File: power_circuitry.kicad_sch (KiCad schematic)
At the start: 29 parts, among them U3 MCP6007, U4 MCP6007, U5 MCP6007

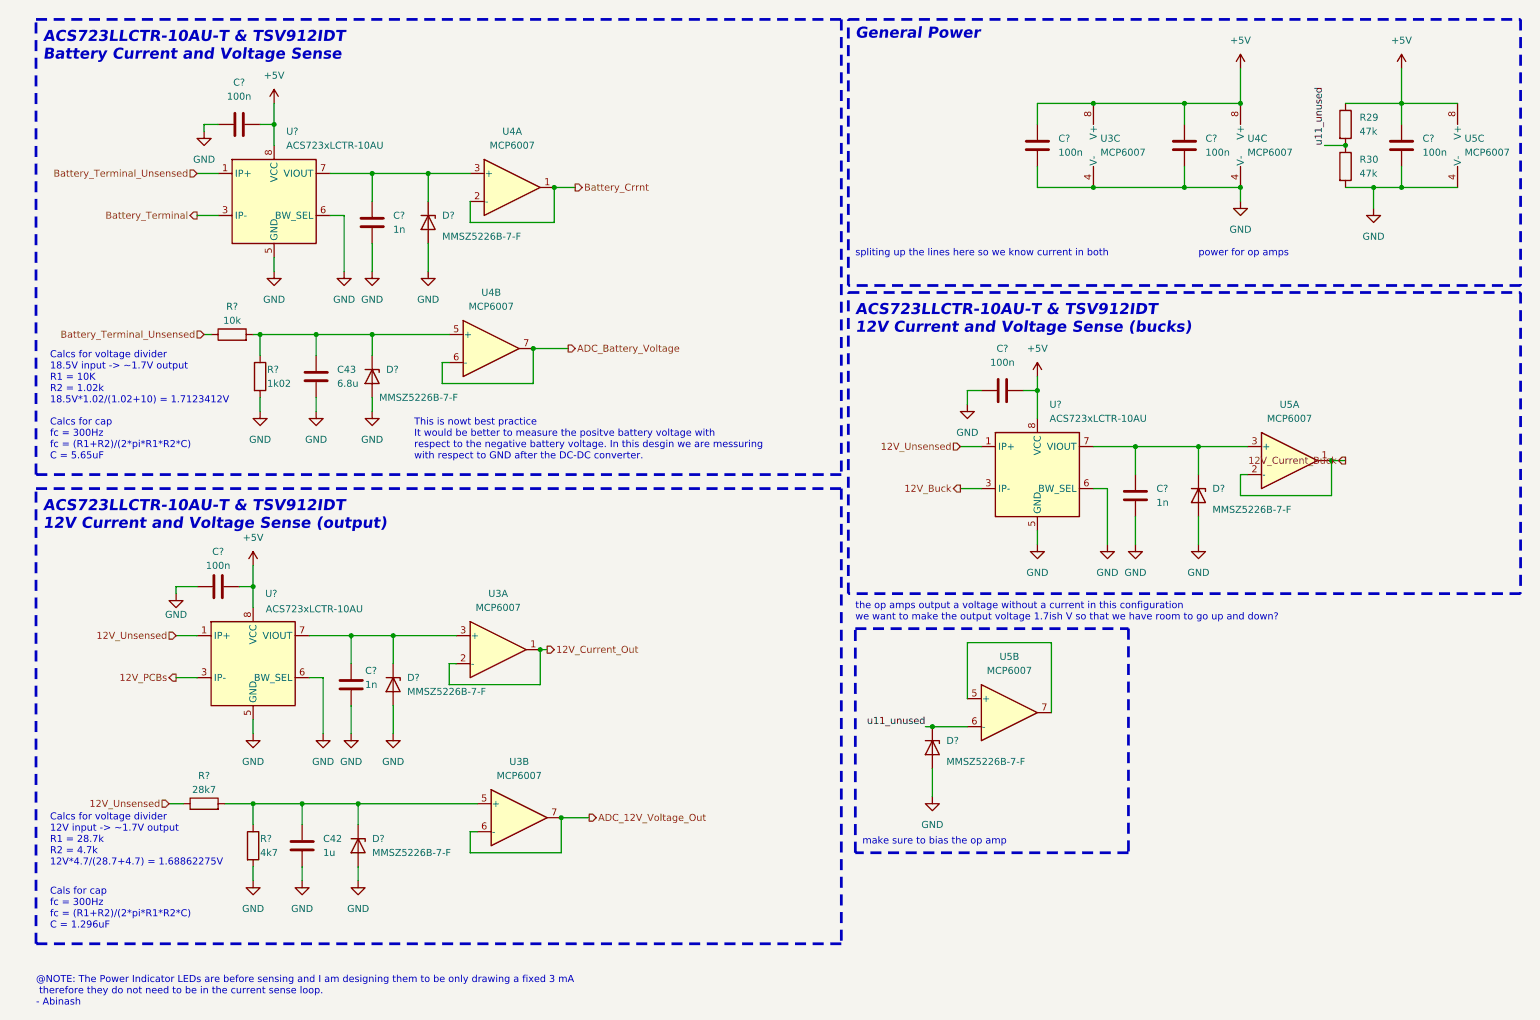
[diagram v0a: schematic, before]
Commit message: buck converter updates
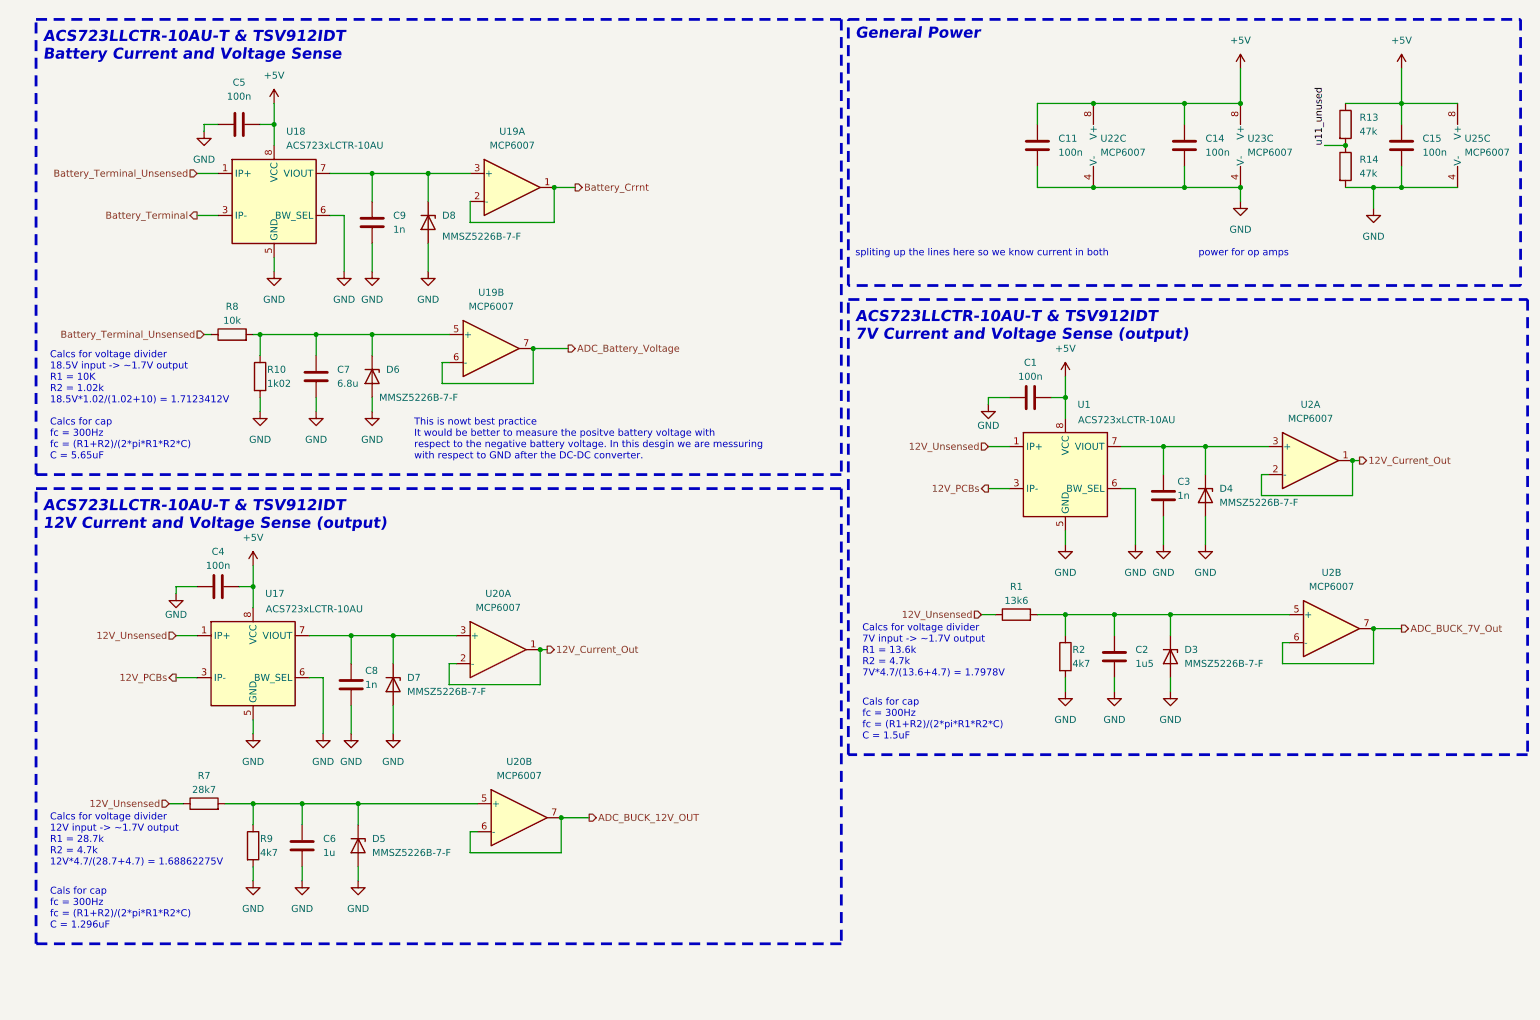
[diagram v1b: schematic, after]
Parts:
- removed C?: 1n, Capacitor_SMD:C_0402_1005Metric, symbol Device:C
- removed C?: 100n, Capacitor_SMD:C_0603_1608Metric, symbol Device:C
- removed D? (x2): MMSZ5226B-7-F, Diode_SMD:D_SOD-123, symbol Device:D_Zener
- removed unit 1 of U5
- removed unit 2 of U5
- removed U?: ACS723xLCTR-10AU, Package_SO:SOIC-8_3.9x4.9mm_P1.27mm, symbol Sensor_Current:ACS723xLCTR-10AU
- added C1: 100n, Capacitor_SMD:C_0603_1608Metric, symbol Device:C
- added C2: 1u5, Capacitor_SMD:C_0603_1608Metric, symbol Device:C
- added C3: 1n, Capacitor_SMD:C_0402_1005Metric, symbol Device:C
- added D3, D4: MMSZ5226B-7-F, Diode_SMD:D_SOD-123, symbol Device:D_Zener
- added R1: 13k6, Resistor_SMD:R_0603_1608Metric, symbol Device:R
- added R2: 4k7, Resistor_SMD:R_0603_1608Metric, symbol Device:R
- added U1: ACS723xLCTR-10AU, Package_SO:SOIC-8_3.9x4.9mm_P1.27mm, symbol Sensor_Current:ACS723xLCTR-10AU
- added U2: MCP6007, Package_SO:SOIC-8_3.9x4.9mm_P1.27mm, symbol ecocad_lib_symbols:MCP6007
- C5: renamed from C?; footprint Capacitor_SMD:C_0402_1005Metric -> Capacitor_SMD:C_0603_1608Metric
- U22: renamed from U3; footprint BP_FTP:SO8_STM -> Package_SO:SOIC-8_3.9x4.9mm_P1.27mm
- U23: renamed from U4; footprint BP_FTP:SO8_STM -> Package_SO:SOIC-8_3.9x4.9mm_P1.27mm
- U25: renamed from U5; footprint BP_FTP:SO8_STM -> Package_SO:SOIC-8_3.9x4.9mm_P1.27mm
- gave numbers to parts that had none: 16
- renumbered C42 to C6, C43 to C7, R29 to R13, R30 to R14, U4 to U19, U3 to U20
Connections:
- net +5V: now also C1.1, U1.8 (VCC)
- net 12V_Current_Out: now also U2.1, U2.2 (-)
- net 12V_PCBs: now also U1.3 (IP-), U1.4 (IP-)
- net 12V_Unsensed: now also R1.1, U1.1 (IP+), U1.2 (IP+)
- net GND: now also C1.2, C2.2, C3.2, D3.2 (A), D4.2 (A), R2.2, U1.5 (GND), U1.6 (BW_SEL)
- net ADC_12V_Voltage_Out renamed ADC_BUCK_12V_OUT
- new net: C3.1, D4.1 (K), U1.7 (VIOUT), U2.3 (+)
- new net: C2.1, D3.1 (K), R1.2, R2.1, U2.5 (+)
- new net ADC_BUCK_7V_Out: U2.6 (-), U2.7
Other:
- note added: "ACS723LLCTR-10AU-T & TSV912IDT 7V Current and Voltage Sense (output)"
- note added: "Calcs for voltage divider 7V input -> ~1.7V output R1 = 13.6k R2 = 4.7k 7V*4.7/(13.6+4.7) = 1.7978V"
- note added: "Cals for cap fc = 300Hz fc = (R1+R2)/(2*pi*R1*R2*C) C = 1.5uF"
- note removed: "@NOTE: The Power Indicator LEDs are before sensing and I am designing them to be only drawing a fixed 3 mA therefore they do not need to be in the current sense loop. - Abinash"
- note removed: "ACS723LLCTR-10AU-T & TSV912IDT 12V Current and Voltage Sense (bucks)"
- note removed: "make sure to bias the op amp"
- note removed: "the op amps output a voltage without a current in this configuration we want to make the output voltage 1.7ish V so that we have room to go up and down?"

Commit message: MCU and Schematic Hierarchy updates
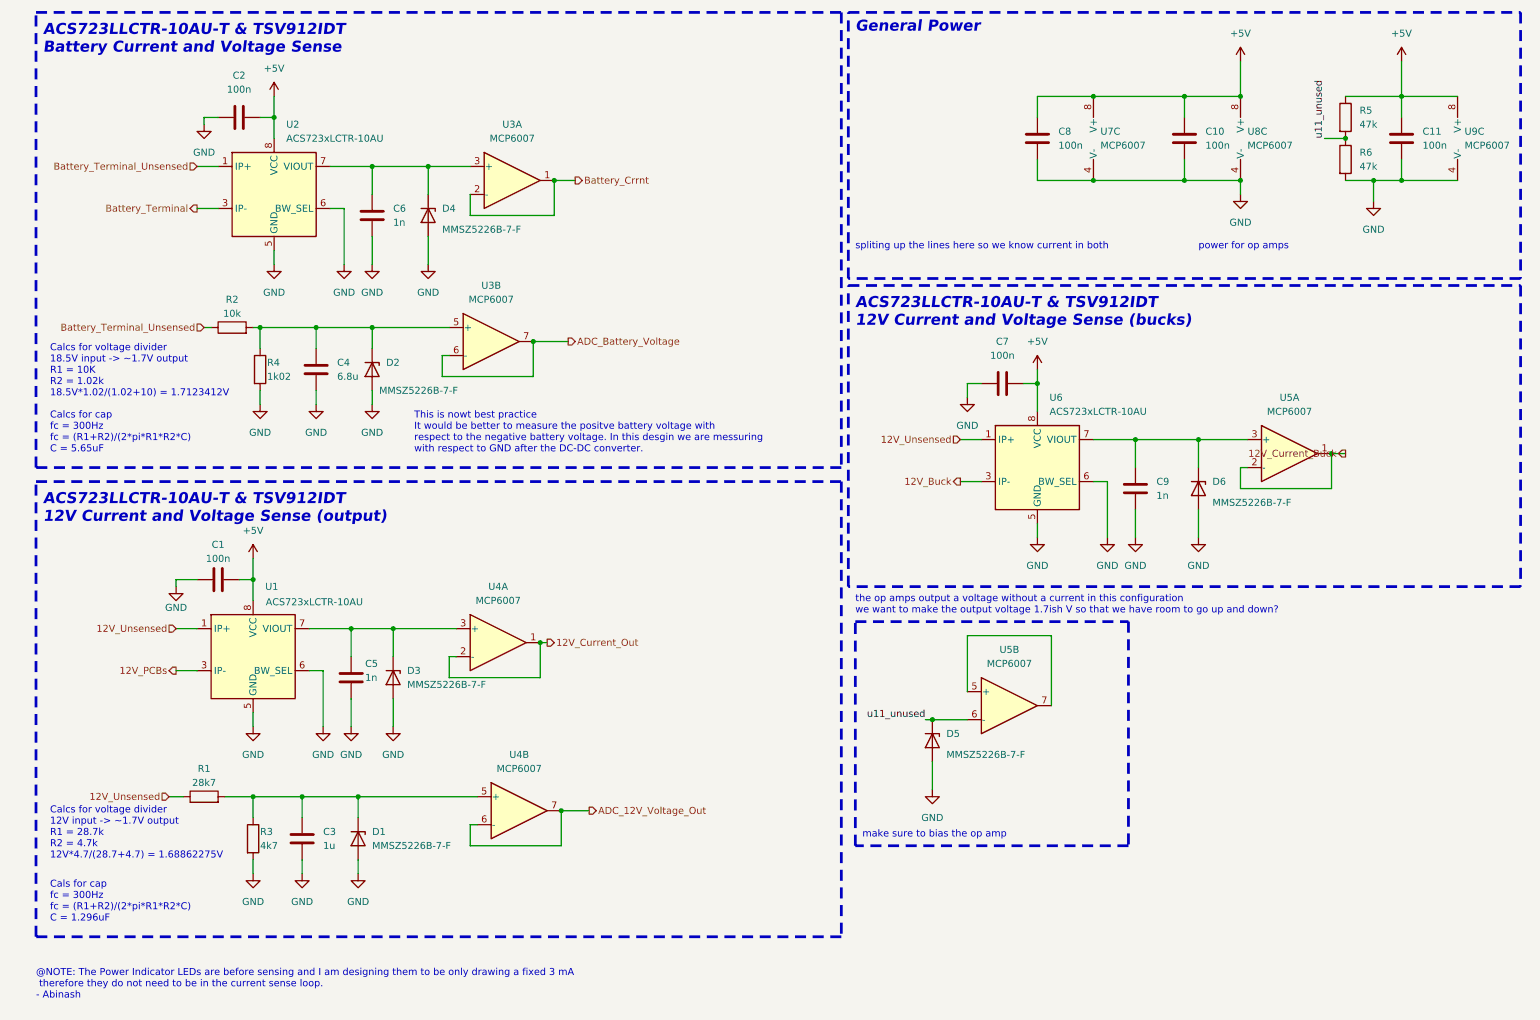
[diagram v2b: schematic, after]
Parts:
- removed C14, C15: 100n, Capacitor_SMD:C_0603_1608Metric, symbol Device:C
- removed D7, D8: MMSZ5226B-7-F, Diode_SMD:D_SOD-123, symbol Device:D_Zener
- removed R10: 1k02, Resistor_SMD:R_0603_1608Metric, symbol Device:R
- removed R13, R14: 47k, Resistor_SMD:R_0805_2012Metric, symbol Device:R
- removed R7: 28k7, Resistor_SMD:R_0603_1608Metric, symbol Device:R
- removed R8: 10k, Resistor_SMD:R_0603_1608Metric, symbol Device:R
- removed R9: 4k7, Resistor_SMD:R_0603_1608Metric, symbol Device:R
- removed U17, U18: ACS723xLCTR-10AU, Package_SO:SOIC-8_3.9x4.9mm_P1.27mm, symbol Sensor_Current:ACS723xLCTR-10AU
- removed U19, U2, U20: MCP6007, Package_SO:SOIC-8_3.9x4.9mm_P1.27mm, symbol ecocad_lib_symbols:MCP6007
- removed U22, U23, U25: MCP6007, Package_SO:SOIC-8_3.9x4.9mm_P1.27mm, symbol Amplifier_Operational:TSV912IDT
- added C10: 100n, Capacitor_SMD:C_0603_1608Metric, symbol Device:C
- added D1, D2: MMSZ5226B-7-F, Diode_SMD:D_SOD-123, symbol Device:D_Zener
- added R3: 4k7, Resistor_SMD:R_0603_1608Metric, symbol Device:R
- added R4: 1k02, Resistor_SMD:R_0603_1608Metric, symbol Device:R
- added R5, R6: 47k, Resistor_SMD:R_0805_2012Metric, symbol Device:R
- added U2, U6: ACS723xLCTR-10AU, Package_SO:SOIC-8_3.9x4.9mm_P1.27mm, symbol Sensor_Current:ACS723xLCTR-10AU
- added U3, U4, U5: MCP6007, Package_SO:SOIC-8_3.9x4.9mm_P1.27mm, symbol ecocad_lib_symbols:MCP6007
- added U7, U8, U9: MCP6007, BP_FTP:SO8_STM, symbol Amplifier_Operational:TSV912IDT
- C2: value 1u5 -> 100n; footprint Capacitor_SMD:C_0603_1608Metric -> Capacitor_SMD:C_0402_1005Metric; Digikey # (none) -> 1276-1043-1-ND; JLCPCB Part#(Optional) C28323 -> C1525; Ordered y -> (none); PCBA (none) -> y
- C3: value 1n -> 1u; footprint Capacitor_SMD:C_0402_1005Metric -> Capacitor_SMD:C_0603_1608Metric; JLCPCB Part#(Optional) C1523 -> C28323; Ordered (none) -> y; PCBA y -> (none)
- C4: value 100n -> 6.8u; Digikey # CC0603KRX7R7BB104 -> (none); JLCPCB Part#(Optional) (none) -> C1631; Ordered y -> (none)
- C5: value 100n -> 1n; footprint Capacitor_SMD:C_0603_1608Metric -> Capacitor_SMD:C_0402_1005Metric; Digikey # 1276-1043-1-ND -> (none); JLCPCB Part#(Optional) C1525 -> C1523
- C6: value 1u -> 1n; footprint Capacitor_SMD:C_0603_1608Metric -> Capacitor_SMD:C_0402_1005Metric; JLCPCB Part#(Optional) C28323 -> C1523; Ordered y -> (none); PCBA (none) -> y
- C7: value 6.8u -> 100n; Digikey # (none) -> CC0603KRX7R7BB104; JLCPCB Part#(Optional) C1631 -> (none); Ordered (none) -> y
- C8: value 1n -> 100n; footprint Capacitor_SMD:C_0402_1005Metric -> Capacitor_SMD:C_0603_1608Metric; Digikey # (none) -> CC0603KRX7R7BB104; JLCPCB Part#(Optional) C1523 -> (none); Ordered (none) -> y; PCBA y -> (none)
- R1: value 13k6 -> 28k7
- R2: value 4k7 -> 10k; Digikey # 311-4.70KHRCT-ND -> RMCF0603FT10K0CT-ND; JLCPCB Part#(Optional) C23164 -> C25804
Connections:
- net +5V: now also C2.2, C7.2, C8.1, C10.1, R5.1, U2.8 (VCC), U6.8 (VCC), U7.8 (V+), U8.8 (V+), U9.8 (V+); no longer C4.1, C5.2
- net 12V_Current_Out: now also U4.1, U4.2 (-)
- net 12V_Unsensed: now also U6.1 (IP+), U6.2 (IP+)
- net ADC_Battery_Voltage: now also U3.6 (-), U3.7
- net Battery_Crrnt: now also U3.1, U3.2 (-)
- net Battery_Terminal: now also U2.3 (IP-), U2.4 (IP-)
- net Battery_Terminal_Unsensed: now also R2.1, U2.1 (IP+), U2.2 (IP+)
- net GND: now also C2.1, C5.2, C7.1, C10.2, D1.2 (A), D2.2 (A), R3.2, R4.2, R6.2, U2.5 (GND), U2.6 (BW_SEL), U6.5 (GND), U6.6 (BW_SEL), U7.4 (V-), U8.4 (V-), U9.4 (V-); no longer C2.2, C5.1, C7.2, R2.2
- net u11_unused: now also D5.1 (K), R5.2, R6.1, U5.6 (-)
- net at D6.1 (K): now also C9.1, U5.3 (+), U6.7 (VIOUT); no longer C7.1
- net at C6.1: now also D4.1 (K), U2.7 (VIOUT), U3.3 (+); no longer D5.1 (K)
- new net: C3.1, D1.1 (K), R1.2, R3.1, U4.5 (+)
- new net: C4.1, D2.1 (K), R2.2, R4.1, U3.5 (+)
- new net: C5.1, D3.1 (K), U1.7 (VIOUT), U4.3 (+)
- new net: U5.5 (+), U5.7
- new net 12V_Buck: U6.3 (IP-), U6.4 (IP-)
- new net 12V_Current_Buck: U5.1, U5.2 (-)
- new net ADC_12V_Voltage_Out: U4.6 (-), U4.7
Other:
- note added: "@NOTE: The Power Indicator LEDs are before sensing and I am designing them to be only drawing a fixed 3 mA therefore they do not need to be in the current sense loop. - Abinash"
- note added: "ACS723LLCTR-10AU-T & TSV912IDT 12V Current and Voltage Sense (bucks)"
- note added: "make sure to bias the op amp"
- note added: "the op amps output a voltage without a current in this configuration we want to make the output voltage 1.7ish V so that we have room to go up and down?"
- note removed: "ACS723LLCTR-10AU-T & TSV912IDT 7V Current and Voltage Sense (output)"
- note removed: "Calcs for voltage divider 7V input -> ~1.7V output R1 = 13.6k R2 = 4.7k 7V*4.7/(13.6+4.7) = 1.7978V"
- note removed: "Cals for cap fc = 300Hz fc = (R1+R2)/(2*pi*R1*R2*C) C = 1.5uF"
